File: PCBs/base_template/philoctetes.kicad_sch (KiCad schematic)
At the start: 176 parts, among them U1 TRRS, U2 TRRS, sw1 Keyswitch, sw10 Keyswitch, sw11 Keyswitch, sw12 Keyswitch, sw13 Keyswitch, sw14 Keyswitch, sw15 Keyswitch, sw16 Keyswitch, sw17 Keyswitch, sw18 Keyswitch, sw19 Keyswitch, sw2 Keyswitch, sw20 Keyswitch, sw21 Keyswitch, sw22 Keyswitch, sw23 Keyswitch, sw24 Keyswitch, sw25 Keyswitch, sw26 Keyswitch, sw27 Keyswitch, sw28 Keyswitch, sw29 Keyswitch, sw3 Keyswitch, sw30 Keyswitch, sw31 Keyswitch, sw32 Keyswitch, sw33 Keyswitch, sw34 Keyswitch, sw35 Keyswitch, sw36 Keyswitch, sw37 Keyswitch, sw38 Keyswitch, sw39 Keyswitch, sw4 Keyswitch, sw40 Keyswitch, sw41 Keyswitch, sw42 Keyswitch, sw5 Keyswitch, sw6 Keyswitch, sw7 Keyswitch, sw8 Keyswitch, sw9 Keyswitch

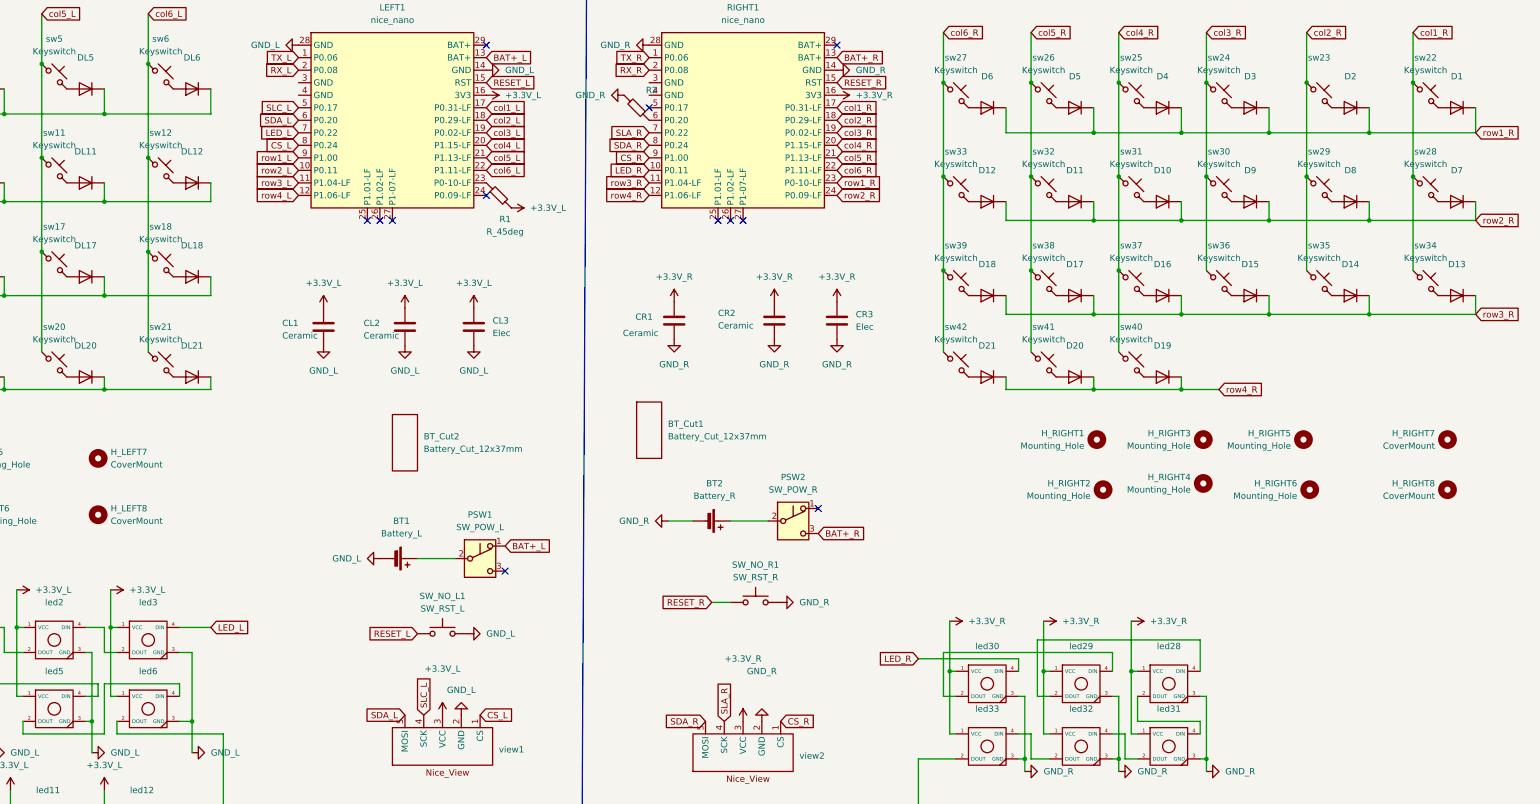
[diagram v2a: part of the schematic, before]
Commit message: worked on edge cuts, made freecad, mirrored, imported to kicad
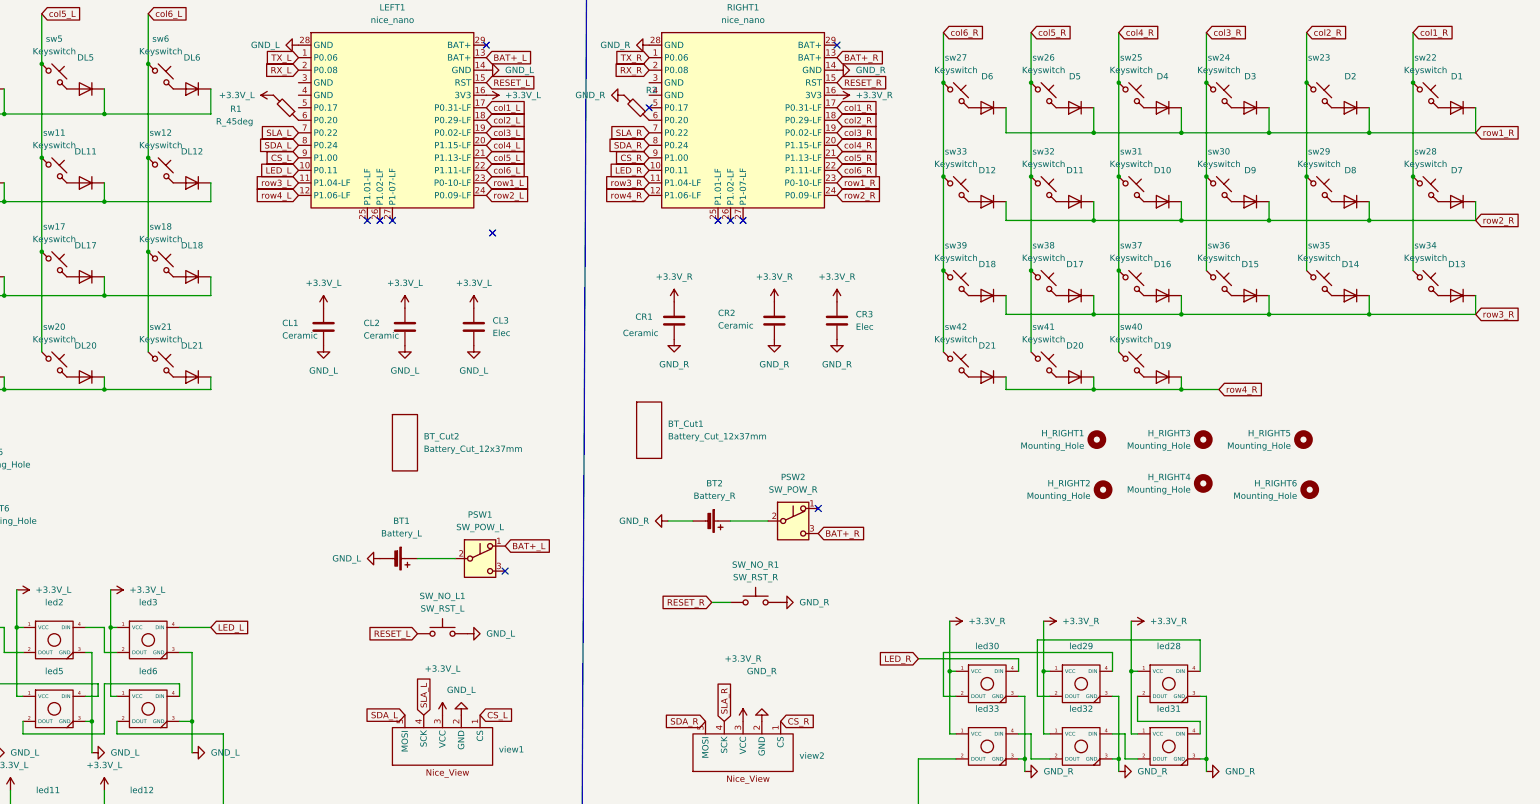
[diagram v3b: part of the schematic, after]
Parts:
- removed H_LEFT7, H_LEFT8, H_RIGHT7, H_RIGHT8: CoverMount, MountingHole:MountingHole_2.2mm_M2_Pad, symbol Mechanical:MountingHole
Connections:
- net CS_L: now also LEFT1.9 (P1.00); no longer LEFT1.8 (P0.24)
- net LED_L: now also LEFT1.10 (P0.11); no longer LEFT1.7 (P0.22)
- net SDA_L: now also LEFT1.8 (P0.24); no longer LEFT1.6 (P0.20)
- net row1_L: now also LEFT1.23 (P0-10-LF); no longer LEFT1.9 (P1.00)
- net row2_L: now also LEFT1.24 (P0.09-LF); no longer LEFT1.10 (P0.11)
- net at R1.1: now also LEFT1.6 (P0.20); no longer LEFT1.23 (P0-10-LF)
- net SLC_L: no longer names the net of LEFT1.5 (P0.17)
- net SLC_L: no longer view1.4 (SCK)
- new net SLA_L: LEFT1.7 (P0.22), view1.4 (SCK)
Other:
- moved on the sheet: R1

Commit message: Finished routing and edge cuts, next up.. check for mistakes.
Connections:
- net GND_L: now also LEFT1.3 (GND), LEFT1.4 (GND)
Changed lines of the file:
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@@
 	)
 	(symbol
+		(lib_id "power:GND")
+		(at 154.94 34.29 270)
+		(unit 1)
+		(exclude_from_sim no)
+		(in_bom yes)
+		(on_board yes)
+		(dnp no)
+		(property "Reference" "#PWR070"
+			(at 148.59 34.29 0)
+			(effects
+				(font
+					(size 1.27 1.27)
+				)
+				(hide yes)
+			)
+		)
+		(property "Value" "GND_L"
+			(at 144.018 31.242 90)
+			(effects
+				(font
+					(size 1.27 1.27)
+				)
+				(justify right)
+			)
+		)
+		(property "Footprint" ""
+			(at 154.94 34.29 0)
+			(effects
+				(font
+					(size 1.27 1.27)
+				)
+				(hide yes)
+			)
+		)
+		(property "Datasheet" ""
+			(at 154.94 34.29 0)
+			(effects
+				(font
+					(size 1.27 1.27)
+				)
+				(hide yes)
+			)
+		)
+		(property "Description" "Power symbol creates a global label with name \"GND\" , ground"
+			(at 154.94 34.29 0)
+			(effects
+				(font
+					(size 1.27 1.27)
+				)
+				(hide yes)
+			)
+		)
+		(pin "1"
+		)
+		(instances
+			(project "philoctetes"
+				(path "/2a55be96-0621-414c-9e2a-5e2757c4c7b6"
+					(reference "#PWR070")
+					(unit 1)
+				)
+			)
+		)
+	)
+	(symbol
 		(lib_id "home:Placeholder_Keyswitch")
 		(at 306.07 34.29 0)
@@
 					(unit 1)
 				)
+			)
+		)
+	)
+	(symbol
+		(lib_id "power:GND")
+		(at 154.94 31.75 270)
+		(unit 1)
+		(exclude_from_sim no)
+		(in_bom yes)
+		(on_board yes)
+		(dnp no)
+		(fields_autoplaced yes)
+		(property "Reference" "#PWR069"
+			(at 148.59 31.75 0)
+			(effects
+				(font
+					(size 1.27 1.27)
+				)
+				(hide yes)
+			)
+		)
+		(property "Value" "GND_L"
+			(at 151.13 31.7499 90)
+			(effects
+				(font
+					(size 1.27 1.27)
+				)
+				(justify right)
+			)
+		)
+		(property "Footprint" ""
+			(at 154.94 31.75 0)
+			(effects
+				(font
+					(size 1.27 1.27)
+				)
+				(hide yes)
+			)
+		)
+		(property "Datasheet" ""
+			(at 154.94 31.75 0)
+			(effects
+				(font
+					(size 1.27 1.27)
+				)
+				(hide yes)
+			)
+		)
+		(property "Description" "Power symbol creates a global label with name \"GND\" , ground"
+			(at 154.94 31.75 0)
+			(effects
+				(font
+					(size 1.27 1.27)
+				)
+				(hide yes)
+			)
+		)
+		(pin "1"
+		)
+		(instances
+			(project "philoctetes"
+				(path "/2a55be96-0621-414c-9e2a-5e2757c4c7b6"
+					(reference "#PWR069")
+					(unit 1)
+				)

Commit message: fixed some routing mistakes, added some clearance for tx/rx, added per led 1nf capacitors (needs to place footprints)
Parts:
- added C1, C10, C11, C12, C13, C14, C15, C16, C17, C18, C19, C2, C20, C21, C22, C23, C24, C25, C26, C27, C28, C29, C3, C30, C31, C32, C33, C34, C35, C36, C37, C38, C39, C4, C40, C41, C42, C43, C44, C45, C46, C47, C48, C49, C5, C50, C51, C52, C53, C54, C6, C7, C8, C9: C_Small, Capacitor_SMD:C_0603_1608Metric_Pad1.08x0.95mm_HandSolder, symbol Device:C_Small
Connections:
- net +3.3V_L: now also C1.1, C10.1, C11.1, C12.1, C13.1, C14.1, C15.1, C16.1, C17.1, C18.1, C19.1, C2.1, C20.1, C21.1, C22.1, C23.1, C24.1, C25.1, C26.1, C27.1, C3.1, C4.1, C5.1, C6.1, C7.1, C8.1, C9.1
- net +3.3V_R: now also C28.2, C29.2, C30.2, C31.1, C32.1, C33.1, C34.2, C35.2, C36.2, C37.2, C38.2, C39.2, C40.2, C41.2, C42.2, C43.2, C44.2, C45.2, C46.2, C47.2, C48.2, C49.2, C50.2, C51.2, C52.2, C53.2, C54.2
- net GND_L: now also C1.2, C10.2, C11.2, C12.2, C13.2, C14.2, C15.2, C16.2, C17.2, C18.2, C19.2, C2.2, C20.2, C21.2, C22.2, C23.2, C24.2, C25.2, C26.2, C27.2, C3.2, C4.2, C5.2, C6.2, C7.2, C8.2, C9.2
- net GND_R: now also C28.1, C29.1, C30.1, C31.2, C32.2, C33.2, C35.1, C36.1, C37.1, C38.1, C39.1, C40.1, C41.1, C42.1, C43.1, C44.1, C45.1, C46.1, C47.1, C48.1, C49.1, C50.1, C51.1, C52.1, C53.1, C54.1
- net at led34.2 (DOUT), led40.4 (DIN): now also C34.1

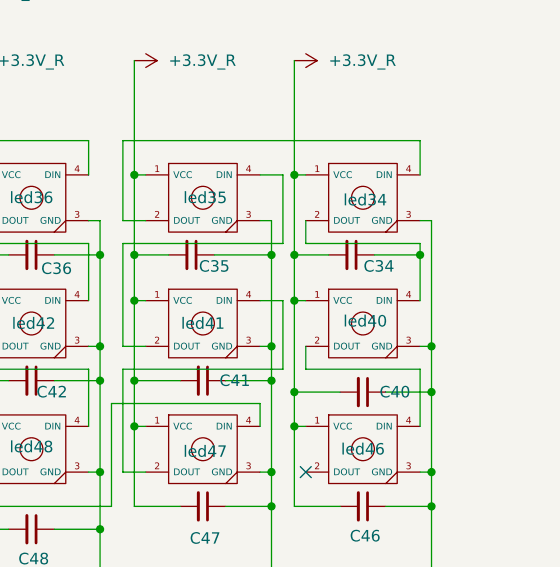
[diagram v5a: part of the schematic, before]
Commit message: placed all 1NF capacitors
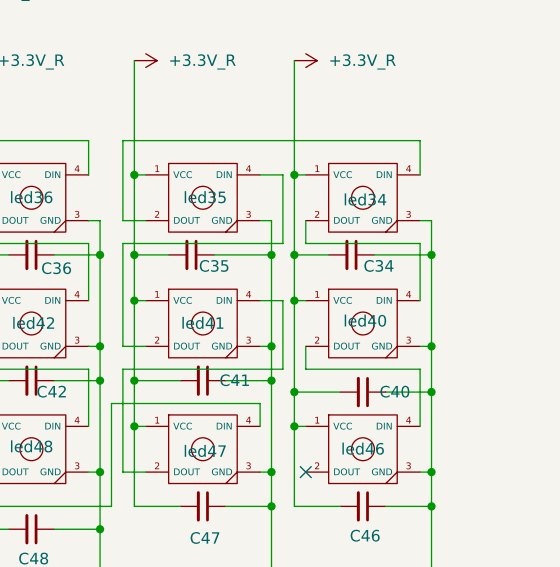
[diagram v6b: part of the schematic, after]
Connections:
- net GND_R: now also C34.1
- net at led34.2 (DOUT), led40.4 (DIN): no longer C34.1
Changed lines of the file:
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@@
 	)
 	(junction
-		(at 391.16 200.66)
-		(diameter 0)
-		(color 0 0 0 0)
-	)
-	(junction
 		(at 303.53 31.75)
 		(diameter 0)
@@
 	)
 	(junction
+		(at 392.43 200.66)
+		(diameter 0)
+		(color 0 0 0 0)
+	)
+	(junction
 		(at 299.72 200.66)
 		(diameter 0)
@@
 	(wire
 		(pts
-			(xy 391.16 200.66) (xy 391.16 205.74)
+			(xy 391.16 199.39) (xy 391.16 205.74)
 		)
 		(stroke
@@
 	(wire
 		(pts
+			(xy 392.43 200.66) (xy 392.43 210.82)
+		)
+		(stroke
+			(width 0)
+			(type default)
+		)
+	)
+	(wire
+		(pts
 			(xy 377.19 215.9) (xy 382.27 215.9)
 		)
@@
 	(wire
 		(pts
-			(xy 391.16 199.39) (xy 391.16 200.66)
-		)
-		(stroke
-			(width 0)
-			(type default)
-		)
-	)
-	(wire
-		(pts
 			(xy 321.31 219.71) (xy 322.58 219.71)
 		)
@@
 	(wire
 		(pts
-			(xy 386.08 200.66) (xy 391.16 200.66)
-		)
-		(stroke
-			(width 0)
-			(type default)
-		)
-	)
-	(wire
-		(pts
 			(xy 359.41 200.66) (xy 359.41 205.74)
 		)
@@
 	(wire
 		(pts
-			(xy 392.43 196.85) (xy 392.43 210.82)
+			(xy 392.43 196.85) (xy 392.43 200.66)
 		)
 		(stroke
@@
 		)
 		(stroke
+			(width 0)
+			(type default)
+		)
+	)
+	(wire
+		(pts
+			(xy 386.08 200.66) (xy 392.43 200.66)
+		)
+		(stroke

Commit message: rotary encoder considerations
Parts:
- added ENC_L1, ENC_R2: RotaryEncoder_Switch, Rotary_Encoder:RotaryEncoder_Alps_EC11E-Switch_Vertical_H20mm, symbol Device:RotaryEncoder_Switch
- added J1, J3: Conn_01x02_Pin, Connector_JST:JST_GH_SM02B-GHS-TB_1x02-1MP_P1.25mm_Horizontal, symbol Connector:Conn_01x02_Pin
- added J2, J4: Conn_01x02_Pin, philoctetes:handwire_A_B, symbol Connector:Conn_01x02_Pin
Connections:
- net GND_L: now also ENC_L1.C
- net GND_R: now also ENC_R2.C
- net col3_L: now also ENC_L1.S1
- net col3_R: now also ENC_R2.S1
- net row4_L: now also ENC_L1.S2
- net row4_R: now also ENC_R2.S2
- new net ENC_LA: ENC_L1.A, J1.2 (Pin_2), J2.2 (Pin_2)
- new net ENC_LB: ENC_L1.B, J1.1 (Pin_1), J2.1 (Pin_1)
- new net ENC_RA: ENC_R2.A, J3.2 (Pin_2), J4.2 (Pin_2)
- new net ENC_RB: ENC_R2.B, J3.1 (Pin_1), J4.1 (Pin_1)
